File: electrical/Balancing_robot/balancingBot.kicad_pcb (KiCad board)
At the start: 2 copper layers, 88 x 64 mm, 32 parts, among them P1 CONN_01X04, P2 CONN_01X04, P3 CONN_01X02, SW1 SW_DIP_x01, U1 DRV8825, U2 DRV8825, U3 WRL-00691, U4 ArduinoProMini, U5 GY-521, U6 D24V10F5

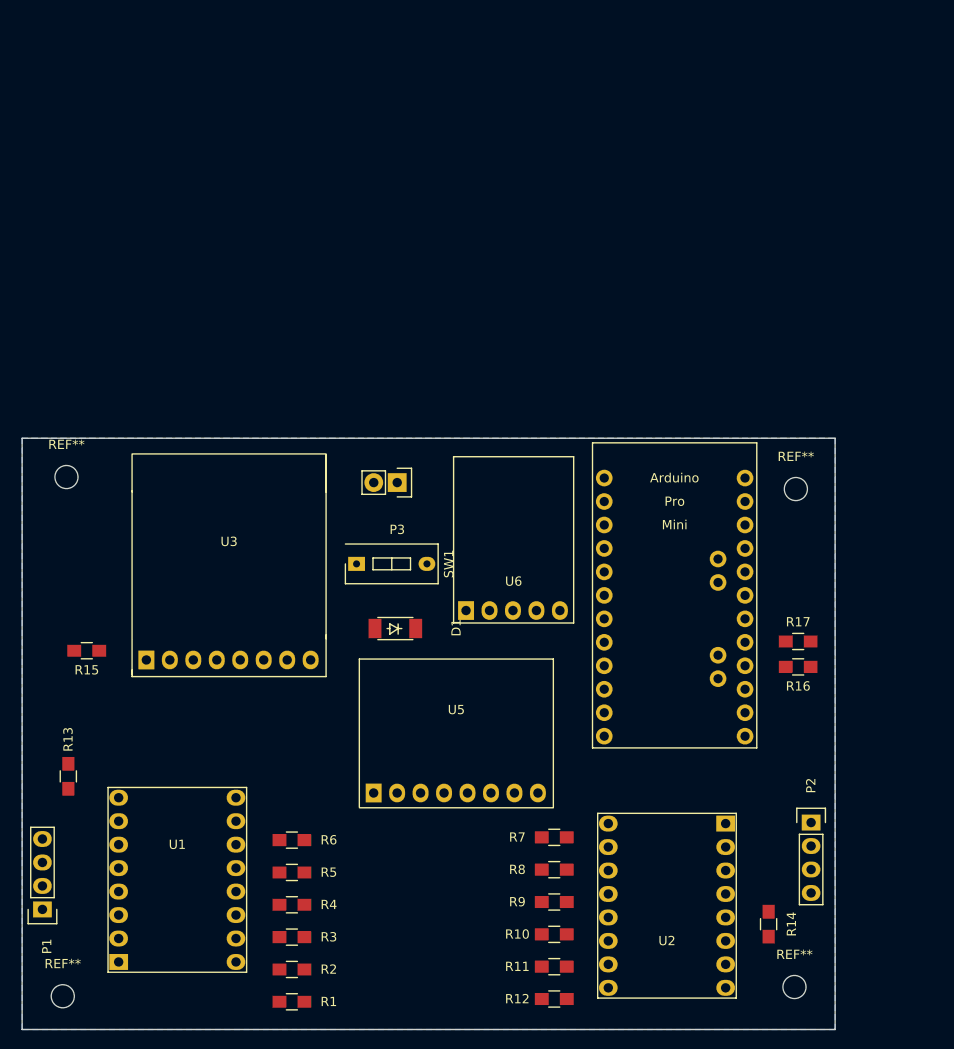
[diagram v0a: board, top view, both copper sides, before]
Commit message: converted to pcb and initial pcb layout
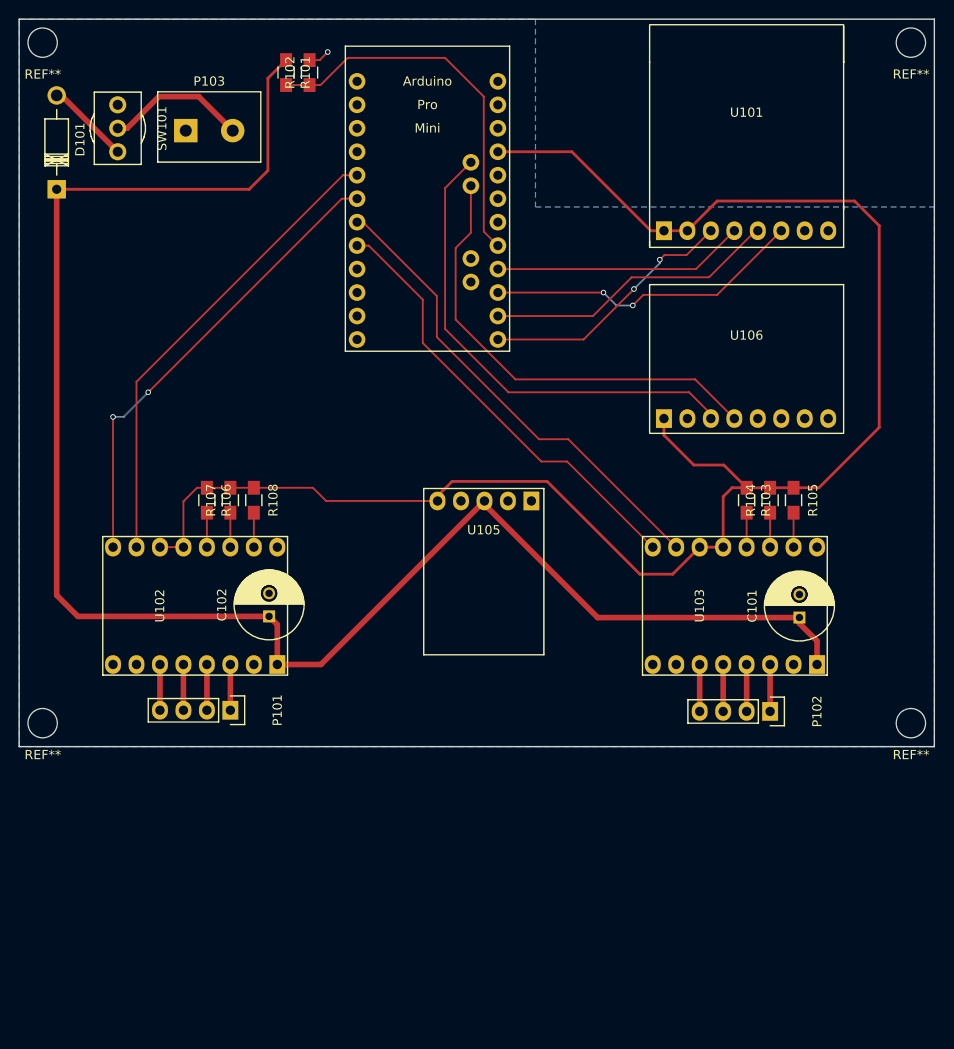
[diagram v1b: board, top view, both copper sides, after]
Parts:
- removed D1: DB2431200L, balancingBot:TMiniP2-F2-B
- removed P1, P2: CONN_01X04, Socket_Strips:Socket_Strip_Straight_1x04
- removed P3: CONN_01X02, Socket_Strips:Socket_Strip_Straight_1x02
- removed R1, R10, R13, R14, R2, R4, R7, R8: NOPOP, Resistors_SMD:R_0805_HandSoldering
- removed R11, R12, R15, R3, R5, R6, R9: 0R, Resistors_SMD:R_0805_HandSoldering
- removed R16: 3K3, Resistors_SMD:R_0805_HandSoldering
- removed R17: 2K2, Resistors_SMD:R_0805_HandSoldering
- removed the REF** at (190.6, 145.4)
- removed the REF** at (111.4, 146.4)
- removed the REF** at (111.8, 90.2)
- removed the REF** at (190.8, 91.5)
- removed SW1: SW_DIP_x01, Buttons_Switches_THT:SW_DIP_x1_Slide
- removed U1, U2: DRV8825, balancingBot:DRV8825
- removed U3: WRL-00691, balancingBot:WRL-00691
- removed U4: ArduinoProMini, balancingBot:Arduino_Pro_Mini
- removed U5: GY-521, balancingBot:GY-521
- removed U6: D24V10F5, balancingBot:D24V10F5
- added C101: 100u, Capacitors_THT:C_Radial_D7.5_L11.2_P2.5, F.Cu at (191.1, 105.4)
- added C102: 100u, Capacitors_THT:C_Radial_D7.5_L11.2_P2.5, F.Cu at (133.7, 105.3)
- added D101: 1N4001, Diodes_THT:Diode_DO-41_SOD81_Horizontal_RM10, F.Cu at (110.7, 59.1)
- added P101: CONN_01X04, Pin_Headers:Pin_Header_Straight_1x04, F.Cu at (129.5, 115.4)
- added P102: CONN_01X04, Pin_Headers:Pin_Header_Straight_1x04, F.Cu at (188.0, 115.6)
- added P103: CONN_01X02, balancingBot:Terminal_Block_200_mil, F.Cu at (127.3, 52.7)
- added R101: 33K, Resistors_SMD:R_0805_HandSoldering, F.Cu at (135.6, 46.4)
- added R102: 21K5, Resistors_SMD:R_0805_HandSoldering, F.Cu at (138.1, 46.4)
- added R103: NOPOP, Resistors_SMD:R_0805_HandSoldering, F.Cu at (185.4, 92.7)
- added R104: 0R, Resistors_SMD:R_0805_HandSoldering, F.Cu at (188.0, 92.7)
- added R105: NOPOP, Resistors_SMD:R_0805_HandSoldering, F.Cu at (190.5, 92.7)
- added R106: NOPOP, Resistors_SMD:R_0805_HandSoldering, F.Cu at (127.0, 92.7)
- added R107: 0R, Resistors_SMD:R_0805_HandSoldering, F.Cu at (129.5, 92.7)
- added R108: NOPOP, Resistors_SMD:R_0805_HandSoldering, F.Cu at (132.1, 92.7)
- added REF**: mounting_hole_0.125in, balancingBot:mounting_hole_0.125in, F.Cu at (109.2, 116.8)
- added REF**: mounting_hole_0.125in, balancingBot:mounting_hole_0.125in, F.Cu at (203.2, 116.8)
- added REF**: mounting_hole_0.125in, balancingBot:mounting_hole_0.125in, F.Cu at (203.2, 43.2)
- added REF**: mounting_hole_0.125in, balancingBot:mounting_hole_0.125in, F.Cu at (109.2, 43.2)
- added SW101: SW_SPDT, balancingBot:SWITCH-200MSP1T1B1M2QEH, F.Cu at (117.3, 52.5)
- added U101: WRL-00691, balancingBot:WRL-00691, F.Cu at (185.4, 53.3)
- added U102: DRV8825, balancingBot:DRV8825, F.Cu at (125.7, 104.1)
- added U103: DRV8825, balancingBot:DRV8825, F.Cu at (184.2, 104.1)
- added U104: ArduinoProMini, balancingBot:Arduino_Pro_Mini, F.Cu at (158.5, 75.3)
- added U105: D24V10F5, balancingBot:D24V10F5, F.Cu at (157.0, 91.4)
- added U106: GY-521, balancingBot:GY-521, F.Cu at (185.4, 77.5)
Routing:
- net 11.75V: track 0.00 -> 185.8 mm
- net +5V: track 0.00 -> 181.3 mm
- net /SCL: track 0.00 -> 52.3 mm
- net /Rstep: track 0.00 -> 51.7 mm
- net /Lstep: track 0.00 -> 51.4 mm
- net /Ldir: track 0.00 -> 50.3 mm, vias 0 -> 2
- net /SDA: track 0.00 -> 49.8 mm
- net /Rdir: track 0.00 -> 48.3 mm
- net Net-(R101-Pad2): track 0.00 -> 41.1 mm
- net /MISO: track 0.00 -> 34.6 mm, vias 0 -> 2
- net /MOSI: track 0.00 -> 32.0 mm
- net /CSN: track 0.00 -> 28.2 mm, vias 0 -> 2
- net /SCK: track 0.00 -> 27.3 mm
- net Net-(P103-Pad2): track 0.00 -> 15.4 mm
- net Net-(D101-Pad2): track 0.00 -> 9.13 mm
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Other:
- board size 88 x 64 mm -> 99.1 x 78.7 mm
- net class Default: clearance 0.2 -> 0.2032; trace_width 0.25 -> 0.2032
- rule trace_clearance: 0.2 -> 0.2032
- rule trace_min: 0.2 -> 0.1524

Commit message: created gerbers
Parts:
- R103, R104, R105, R106, R107, R108: moved to B.Cu
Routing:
- net (no net): track 0.00 -> 5.08 mm
- net +5V: track 181.3 -> 183.6 mm, vias 0 -> 2
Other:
- board text added: "Balancing Bot Rev. 0 Alan Ford"

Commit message: updated pcb to include status LED, associated resistor, and radio enable line
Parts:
- added D102: Red LED, LEDs:LED_0805_HandSoldering, F.Cu at (164.8, 64.3)
- added R109: 330R, Resistors_SMD:R_0805_HandSoldering, F.Cu at (168.0, 64.3)
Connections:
- SW101 pad 3: (no net) -> Net-(SW101-Pad3)
- U101 pad 2: +5V -> /CE
- U101 pad 7: (no net) -> Net-(U101-Pad7)
- U102 pad 10: /Lstep -> /Rstep
- U102 pad 16: (no net) -> Net-(U102-Pad16)
- U102 pad 7: (no net) -> Net-(U102-Pad7)
- U102 pad 9: /Ldir -> /Rdir
- U103 pad 10: /Rstep -> /Lstep
- U103 pad 16: (no net) -> Net-(U103-Pad16)
- U103 pad 7: (no net) -> Net-(U103-Pad7)
- U103 pad 9: /Rdir -> /Ldir
- U104 pad 1: (no net) -> Net-(U104-Pad1)
- U104 pad 10: (no net) -> Net-(U104-Pad10)
- U104 pad 11: (no net) -> Net-(U104-Pad11)
- U104 pad 12: (no net) -> /CE
- U104 pad 18: (no net) -> Net-(U104-Pad18)
- U104 pad 19: (no net) -> Net-(U104-Pad19)
- U104 pad 2: (no net) -> Net-(U104-Pad2)
- U104 pad 20: (no net) -> Net-(D102-Pad2)
- U104 pad 22: (no net) -> Net-(U104-Pad22)
- U104 pad 24: (no net) -> Net-(U104-Pad24)
- U104 pad 3: (no net) -> Net-(U104-Pad3)
- U104 pad 33: (no net) -> Net-(U104-Pad33)
- U104 pad 34: (no net) -> Net-(U104-Pad34)
- U104 pad 5: /Lstep -> /Rstep
- U104 pad 6: /Ldir -> /Rdir
- U104 pad 7: /Rstep -> /Lstep
- U104 pad 8: /Rdir -> /Ldir
- U104 pad 9: (no net) -> Net-(U104-Pad9)
- U105 pad 1: (no net) -> Net-(U105-Pad1)
- U105 pad 2: (no net) -> Net-(U105-Pad2)
- U106 pad 5: (no net) -> Net-(U106-Pad5)
- U106 pad 6: (no net) -> Net-(U106-Pad6)
- U106 pad 7: (no net) -> Net-(U106-Pad7)
- U106 pad 8: (no net) -> Net-(U106-Pad8)
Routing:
- net /CE: track 0.00 -> 70.7 mm, vias 0 -> 2
- net +5V: track 183.6 -> 126.9 mm, vias 2 -> 1
- net Net-(D102-Pad2): track 0.00 -> 9.48 mm
- net Net-(D102-Pad1): track 0.00 -> 3.16 mm
- net GND: track 2.33 -> 4.69 mm, vias 1 -> 2
- net /Rdir: track 48.3 -> 50.3 mm, vias 0 -> 2
- net /Ldir: track 50.3 -> 48.3 mm, vias 2 -> 0

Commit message: rerouted power and moved traces hidden by daughter boards
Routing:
- net +5V: track 126.9 -> 153.7 mm
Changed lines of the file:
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@@
   (general
     (links 63)
-    (no_connects 1)
-    (area 106.604999 40.564999 205.815001 119.455001)
+    (no_connects 0)
+    (area 100.348543 38.2013 212.020658 121.35228)
     (thickness 1.6)
     (drawings 5)
-    (tracks 168)
+    (tracks 174)
     (zones 0)
     (modules 27)
@@
   )
   (setup
-    (last_trace_width 0.2032)
+    (last_trace_width 0.3048)
     (user_trace_width 0.3048)
     (user_trace_width 0.6096)
@@
   (segment (start 139.3025 47.7685) (end 142.24 44.831) (width 0.2032) (layer F.Cu) (net 15))
   (segment (start 135.5725 47.7685) (end 138.1125 47.7685) (width 0.2032) (layer F.Cu) (net 15))
+  (segment (start 180.34 97.79) (end 182.88 97.79) (width 0.3048) (layer B.Cu) (net 16) (status C00000))
+  (segment (start 176.47 83.87) (end 172.8732 83.87) (width 0.3048) (layer B.Cu) (net 16))
+  (segment (start 177.9778 65.0478) (end 176.47 63.54) (width 0.3048) (layer B.Cu) (net 16))
+  (segment (start 177.9778 71.12) (end 177.9778 65.0478) (width 0.3048) (layer B.Cu) (net 16))
+  (segment (start 172.7327 76.3651) (end 177.9778 71.12) (width 0.3048) (layer B.Cu) (net 16))
+  (segment (start 172.7327 83.7295) (end 172.7327 76.3651) (width 0.3048) (layer B.Cu) (net 16))
+  (segment (start 172.8732 83.87) (end 172.7327 83.7295) (width 0.3048) (layer B.Cu) (net 16))
   (segment (start 187.96 91.36) (end 185.42 91.36) (width 0.3048) (layer B.Cu) (net 16))
   (segment (start 190.5 91.36) (end 187.96 91.36) (width 0.3048) (layer B.Cu) (net 16))
@@
   (segment (start 180.34 91.313) (end 176.47 87.443) (width 0.3048) (layer F.Cu) (net 16))
   (segment (start 185.42 91.36) (end 184.611 91.36) (width 0.3048) (layer B.Cu) (net 16))
+  (segment (start 182.88 93.091) (end 182.88 97.79) (width 0.3048) (layer B.Cu) (net 16))
   (segment (start 184.611 91.36) (end 182.88 93.091) (width 0.3048) (layer B.Cu) (net 16))
-  (segment (start 182.88 93.091) (end 182.88 97.79) (width 0.3048) (layer B.Cu) (net 16))
   (segment (start 127 91.36) (end 125.556 91.36) (width 0.3048) (layer B.Cu) (net 16))
   (segment (start 124.46 92.456) (end 124.46 97.79) (width 0.3048) (layer B.Cu) (net 16))
@@
   (segment (start 136.605 92.79) (end 135.128 91.313) (width 0.3048) (layer F.Cu) (net 16))
   (segment (start 176.47 63.54) (end 175.046 63.54) (width 0.3048) (layer F.Cu) (net 16))
+  (segment (start 175.046 63.54) (end 166.497 54.991) (width 0.3048) (layer F.Cu) (net 16))
   (segment (start 166.497 54.991) (end 158.496 54.991) (width 0.3048) (layer F.Cu) (net 16))
-  (segment (start 175.046 63.54) (end 166.497 54.991) (width 0.3048) (layer F.Cu) (net 16))
-  (segment (start 180.34 97.79) (end 182.88 97.79) (width 0.3048) (layer F.Cu) (net 16))
   (segment (start 151.962 92.79) (end 151.962 92.259) (width 0.3048) (layer F.Cu) (net 16))
   (segment (start 151.962 92.259) (end 153.543 90.678) (width 0.3048) (layer F.Cu) (net 16))

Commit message: changed stepper drivers to A4988 on pcb and schematic
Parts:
- U102, U103: value DRV8825 -> A4988; footprint balancingBot:DRV8825 -> balancingBot:A4988
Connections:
- U102 pad 7: Net-(U102-Pad7) -> +5V
- U103 pad 7: Net-(U103-Pad7) -> +5V
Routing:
- net +5V: track 153.7 -> 181.2 mm
